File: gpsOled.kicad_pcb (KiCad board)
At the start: 2 copper layers, 38 x 60 mm, 6 parts, among them SW3 SW_Push, U1 MT3608, U2 ESP32-WROOM-E

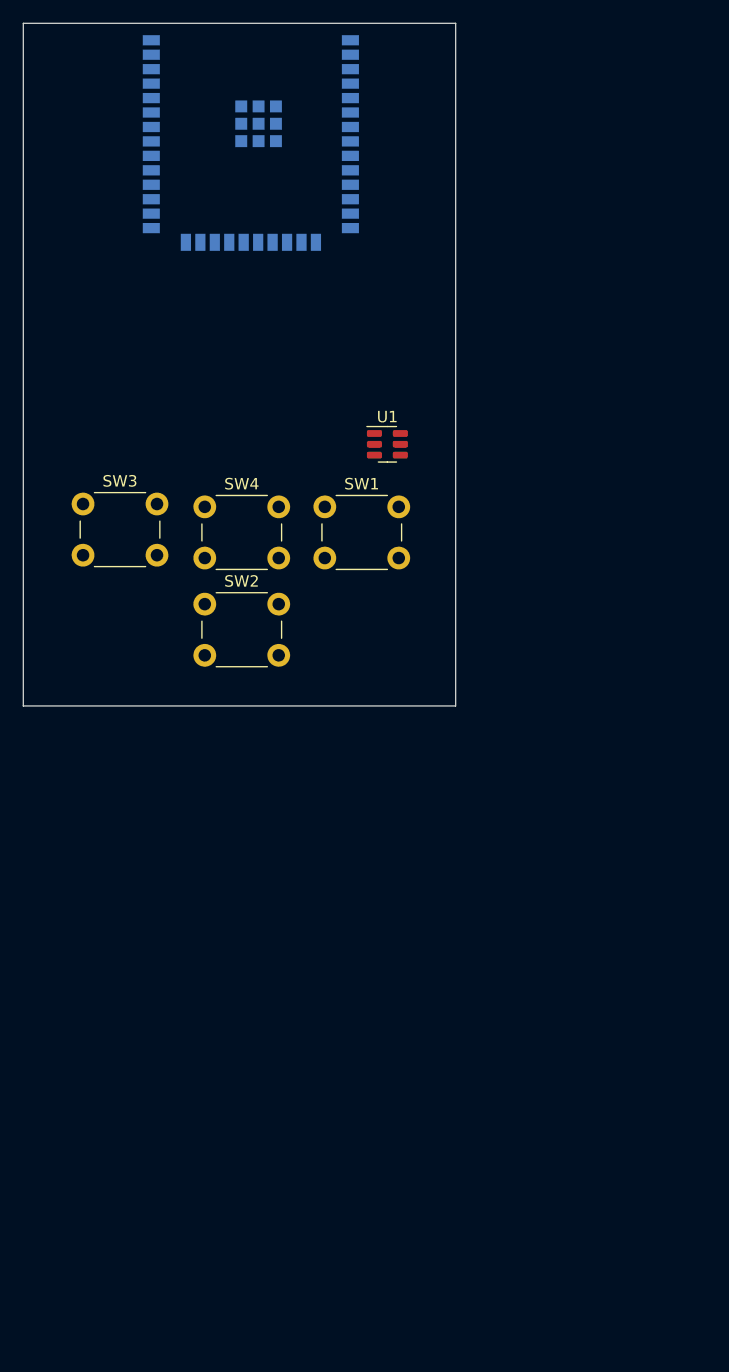
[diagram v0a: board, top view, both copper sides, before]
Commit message: parcialmente terminada PCB falta verificar tamano de componentes
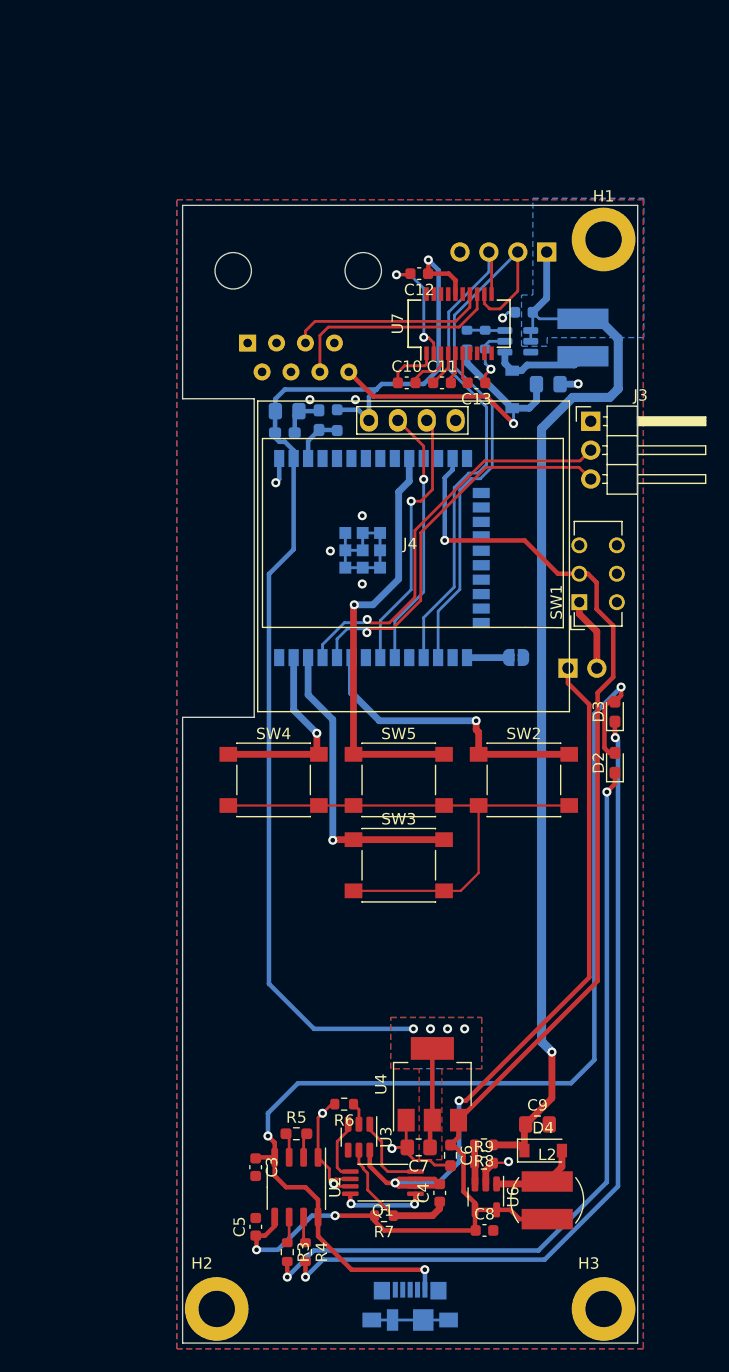
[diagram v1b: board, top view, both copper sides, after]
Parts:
- added C1: 22uF, Capacitor_SMD:C_0603_1608Metric, B.Cu at (156.0, 68.4)
- added C10: C, Capacitor_SMD:C_0603_1608Metric, F.Cu at (145.7, 74.6)
- added C11: ~, Capacitor_SMD:C_0603_1608Metric, F.Cu at (148.8, 74.6)
- added C12: ~, Capacitor_SMD:C_0603_1608Metric, F.Cu at (146.8, 65.0)
- added C13: ~, Capacitor_SMD:C_0603_1608Metric, F.Cu at (151.8, 74.6)
- added C14: 100nF, Capacitor_SMD:C_0603_1608Metric_Pad1.08x0.95mm_HandSolder, B.Cu at (138.0, 77.9)
- added C15: 22uF, Capacitor_SMD:C_0805_2012Metric_Pad1.18x1.45mm_HandSolder, B.Cu at (135.2, 77.1)
- added C16: 100nF, Capacitor_SMD:C_0603_1608Metric_Pad1.08x0.95mm_HandSolder, B.Cu at (135.0, 79.0)
- added C2: 22uF, Capacitor_SMD:C_0805_2012Metric_Pad1.18x1.45mm_HandSolder, B.Cu at (158.1, 74.7)
- added C3: 0.1uF, Capacitor_SMD:C_0603_1608Metric, F.Cu at (132.4, 143.5)
- added C4: 0.1uF, Capacitor_SMD:C_0603_1608Metric, F.Cu at (148.6, 145.8)
- added C5: 10uF, Capacitor_SMD:C_0603_1608Metric, F.Cu at (132.4, 148.8)
- added C6: 0.1uF, Resistor_SMD:R_0603_1608Metric_Pad0.98x0.95mm_HandSolder, F.Cu at (149.6, 142.5)
- added C7: 10uF, Resistor_SMD:R_0805_2012Metric_Pad1.20x1.40mm_HandSolder, F.Cu at (146.8, 141.8)
- added C8: ~, Capacitor_SMD:C_0603_1608Metric, F.Cu at (152.5, 149.1)
- added C9: ~, Capacitor_SMD:C_0805_2012Metric_Pad1.18x1.45mm_HandSolder, F.Cu at (157.2, 139.8)
- added D1: SS34, Diode_SMD:D_SOD-123, B.Cu at (155.0, 75.2)
- added D2: B, LED_SMD:LED_0603_1608Metric_Pad1.05x0.95mm_HandSolder, F.Cu at (164.0, 108.0)
- added D3: R, LED_SMD:LED_0603_1608Metric_Pad1.05x0.95mm_HandSolder, F.Cu at (164.0, 103.5)
- added D4: ~, Diode_SMD:D_SOD-123, F.Cu at (157.7, 142.1)
- added H1: MountingHole, MountingHole:MountingHole_3.2mm_M3_DIN965_Pad, F.Cu at (163.0, 62.0)
- added H2: MountingHole, MountingHole:MountingHole_3.2mm_M3_DIN965_Pad, F.Cu at (129.0, 156.0)
- added H3: MountingHole, MountingHole:MountingHole_3.2mm_M3_DIN965_Pad, F.Cu at (163.0, 156.0)
- added J1: USB_B_Micro, Connector_USB:USB_Micro-B_Molex_47346-0001, B.Cu at (146.0, 155.8)
- added J2: Conn_01x02, Connector_PinHeader_2.54mm:PinHeader_1x02_P2.54mm_Vertical, B.Cu at (159.9, 99.7)
- added J3: Conn_01x03, Connector_PinHeader_2.54mm:PinHeader_1x03_P2.54mm_Horizontal, F.Cu at (161.9, 78.0)
- added J4: SSD1306, MSS_Devices:128x64OLED, F.Cu at (146.0, 88.5)
- added J5: RJ45, Connector_RJ:RJ45_Amphenol_54602-x08_Horizontal, B.Cu at (131.7, 71.1)
- added J6: Conn_01x04, Connector_PinHeader_2.54mm:PinHeader_1x04_P2.54mm_Horizontal, B.Cu at (158.0, 63.1)
- added JP1: Jumper_2_Open, Jumper:SolderJumper-2_P1.3mm_Open_RoundedPad1.0x1.5mm, B.Cu at (155.3, 98.7)
- added L1: 22uH, MSS_Devices:L_Bourns_SDR0403, B.Cu at (161.2, 70.6)
- added L2: ~, MSS_Devices:L_Bourns_SDR0403, F.Cu at (158.1, 146.4)
- added Q1: FS8205A, Package_SO:TSSOP-8_4.4x3mm_P0.65mm, F.Cu at (143.6, 144.9)
- added R1: R, Resistor_SMD:R_0603_1608Metric, B.Cu at (151.0, 70.8)
- added R10: 10k, Resistor_SMD:R_0603_1608Metric_Pad0.98x0.95mm_HandSolder, B.Cu at (139.6, 77.9)
- added R2: 2.2k, Resistor_SMD:R_0603_1608Metric, B.Cu at (152.6, 70.8)
- added R3: 1k, Resistor_SMD:R_0603_1608Metric, F.Cu at (135.2, 151.0)
- added R4: 1k, Resistor_SMD:R_0603_1608Metric, F.Cu at (136.8, 151.0)
- added R5: 1.2k, Resistor_SMD:R_0603_1608Metric_Pad0.98x0.95mm_HandSolder, F.Cu at (136.0, 140.6)
- added R6: 1k, Resistor_SMD:R_0603_1608Metric, F.Cu at (140.2, 138.0)
- added R7: 100, Resistor_SMD:R_0603_1608Metric, F.Cu at (143.7, 147.8)
- added R8: ~, Resistor_SMD:R_0603_1608Metric, F.Cu at (152.5, 141.6)
- added R9: ~, Resistor_SMD:R_0603_1608Metric, F.Cu at (152.5, 143.2)
- added SW1: on/off, Button_Switch_THT:SW_CuK_JS202011AQN_DPDT_Angled, F.Cu at (160.9, 93.9)
- added U2: TP4056, Package_SO:SOP-8_3.9x4.9mm_P1.27mm, F.Cu at (136.0, 145.3)
- added U3: DW01A, Package_TO_SOT_SMD:SOT-23-6, F.Cu at (141.5, 140.9)
- added U4: AP1117-33, Package_TO_SOT_SMD:SOT-223-3_TabPin2, F.Cu at (147.9, 136.2)
- added U6: MIC2251, Package_TO_SOT_SMD:SOT-23-5, F.Cu at (152.7, 146.2)
- added U7: MAX3232, Package_SO:SSOP-20_3.9x8.7mm_P0.635mm, F.Cu at (150.3, 69.4)
- SW2: renamed from SW1; footprint Button_Switch_THT:SW_PUSH_6mm -> Button_Switch_SMD:SW_SPST_PTS645
- SW3: renamed from SW2; footprint Button_Switch_THT:SW_PUSH_6mm -> Button_Switch_SMD:SW_SPST_PTS645
- SW4: renamed from SW3; footprint Button_Switch_THT:SW_PUSH_6mm -> Button_Switch_SMD:SW_SPST_PTS645
- SW5: renamed from SW4; footprint Button_Switch_THT:SW_PUSH_6mm -> Button_Switch_SMD:SW_SPST_PTS645
- U1: moved to B.Cu
- moved U5 39.7 mm to (141.5, 90.0), turned to -90 degrees
- moved SW2 29.7 mm to (156.0, 109.5)
- moved SW4 29.5 mm to (134.0, 109.5)
- moved SW5 29.4 mm to (145.0, 109.5)
- moved SW3 28.6 mm to (145.0, 117.0)
- moved U1 14.6 mm to (155.5, 71.0)
- renumbered U2 to U5
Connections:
- net /charger/VOUT_5V renamed +5V
- U5 pad 1: unconnected-(U2-Pad1) -> GND
- U5 pad 13: unconnected-(U2-Pad13) -> /batt_status
- U5 pad 15: unconnected-(U2-Pad15) -> GND
- U5 pad 2: unconnected-(U2-Pad2) -> +3V3
- U5 pad 25: unconnected-(U2-Pad25) -> Net-(U5-Pad25)
- U5 pad 3: unconnected-(U2-Pad3) -> /ESP32/RST
- U5 pad 38: unconnected-(U2-Pad38) -> GND
- U5 pad 39: unconnected-(U2-Pad39) -> GND
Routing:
- net /batt_status: track 0.00 -> 119.0 mm, vias 0 -> 3
- net +3V3: track 0.00 -> 113.1 mm, vias 0 -> 5
- net GND: track 0.00 -> 110.6 mm, vias 0 -> 13
- net /charger/VBUS: track 0.00 -> 99.6 mm, vias 0 -> 3
- net +5V: track 0.00 -> 99.5 mm, vias 0 -> 1
- net Net-(D3-Pad1): track 0.00 -> 73.1 mm, vias 0 -> 2
- net Net-(D2-Pad1): track 0.00 -> 69.2 mm, vias 0 -> 2
- net /charger/BAT-: track 0.00 -> 68.3 mm, vias 0 -> 2
- net /ESP32/UART_RX_2: track 0.00 -> 49.8 mm
- net /ESP32/UART_TX_2: track 0.00 -> 45.1 mm
- net Net-(SW5-Pad1): track 0.00 -> 37.0 mm, vias 0 -> 1
- net /ESP32/UART_TX_0: track 0.00 -> 35.5 mm, vias 0 -> 1
- net /ESP32/UART_RX_0: track 0.00 -> 34.4 mm, vias 0 -> 1
- net +12V: track 0.00 -> 28.5 mm, vias 0 -> 1
- net Net-(SW3-Pad1): track 0.00 -> 26.7 mm, vias 0 -> 1
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- added copper zone on B.Cu, net +3V3
- added copper zone on F.Cu, net +3V3
- added copper zone on B.Cu, net +5V
- added copper zone on B.Cu, net GND
- added copper zone on F.Cu, net GND
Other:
- board size 38 x 60 mm -> 40 x 100 mm
- board text added: "BATTERY 3.7V"
